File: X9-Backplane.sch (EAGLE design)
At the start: 15 parts

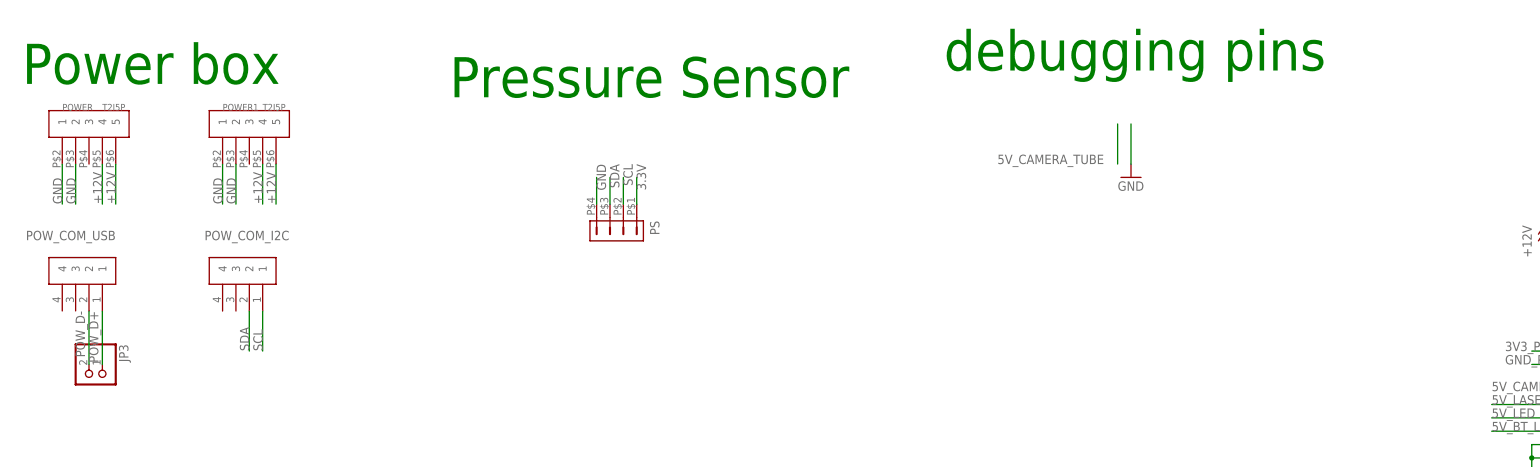
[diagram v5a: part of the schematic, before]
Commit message: added a lot of silk screen
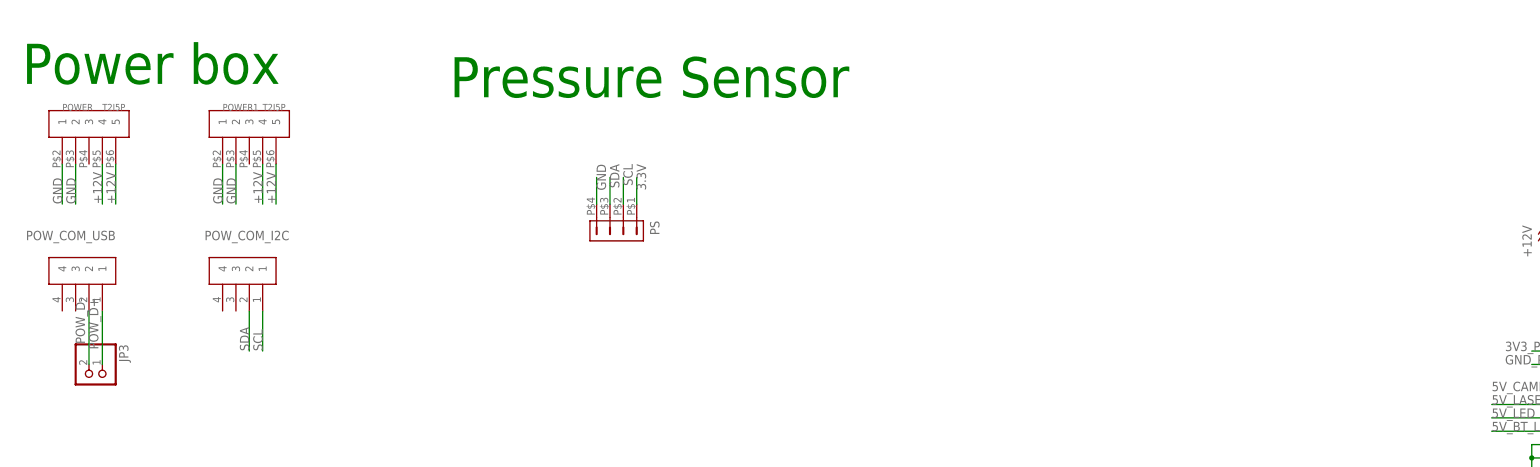
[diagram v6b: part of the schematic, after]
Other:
- note removed: "debugging pins"
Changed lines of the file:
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@@
 <part name="GND2" library="supply1" deviceset="GND" device=""/>
 <part name="PS" library="con-hirose-df13" deviceset="DF13-4P-1.25" device="DSA"/>
-<part name="GND3" library="SparkFun-Aesthetics" deviceset="GND" device=""/>
 <part name="POW_COM_USB" library="BACKPLANE" deviceset="T2I" device=""/>
 <part name="JP3" library="pinhead" deviceset="PINHD-1X2" device=""/>
@@
 <sheet>
 <plain>
-<text x="195.58" y="200.66" size="7.62" layer="91">debugging pins</text>
 <text x="208.28" y="88.9" size="7.62" layer="91">Blue tooth</text>
 <text x="104.14" y="116.84" size="7.62" layer="91">Cammera tube</text>
@@
 <attribute name="NAME" x="139.7" y="172.085" size="1.778" layer="95" rot="R270"/>
 </instance>
-<instance part="GND3" gate="1" x="231.14" y="180.34"/>
 <instance part="POW_COM_USB" gate="G$1" x="38.1" y="167.64" smashed="yes" rot="R180">
 <attribute name="NAME" x="38.1" y="170.18" size="1.778" layer="95" rot="R180"/>
@@
 </segment>
 <segment>
-<wire x1="231.14" y1="190.5" x2="231.14" y2="182.88" width="0.1524" layer="91"/>
-<pinref part="GND3" gate="1" pin="GND"/>
-</segment>
-<segment>
 <pinref part="SC1" gate="G$1" pin="3"/>
 <wire x1="195.58" y1="68.58" x2="195.58" y2="76.2" width="0.1524" layer="91"/>
@@
 <label x="132.08" y="55.88" size="1.778" layer="95" rot="R90"/>
 </segment>
-<segment>
-<wire x1="228.6" y1="190.5" x2="228.6" y2="182.88" width="0.1524" layer="91"/>
-<label x="205.74" y="182.88" size="1.778" layer="95"/>
-</segment>
 </net>
 <net name="5V_BT_LED" class="0">
@@
 <pinref part="JP3" gate="G$1" pin="1"/>
 <wire x1="35.56" y1="144.78" x2="35.56" y2="154.94" width="0.1524" layer="91"/>
-<label x="33.02" y="154.94" size="1.778" layer="95" rot="R270"/>
+<label x="33.02" y="157.48" size="1.778" layer="95" rot="R270"/>
 </segment>
 </net>
@@
 <pinref part="JP3" gate="G$1" pin="2"/>
 <wire x1="33.02" y1="144.78" x2="33.02" y2="154.94" width="0.1524" layer="91"/>
-<label x="30.48" y="154.94" size="1.778" layer="95" rot="R270"/>
-</segment>
-</net>
+<label x="30.48" y="157.48" size="1.778" layer="95" rot="R270"/>
+</segment>
+</net>
